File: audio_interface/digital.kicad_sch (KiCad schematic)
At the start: 45 parts, among them J10 MIC_EXT, J11 INST_EXT, J13 Test Headers, J14 SWD, J15 PCM_Jumper, J16 USB_B, SW1 SW_Push, U10 PCM4202, U11 STM32F042K6Tx

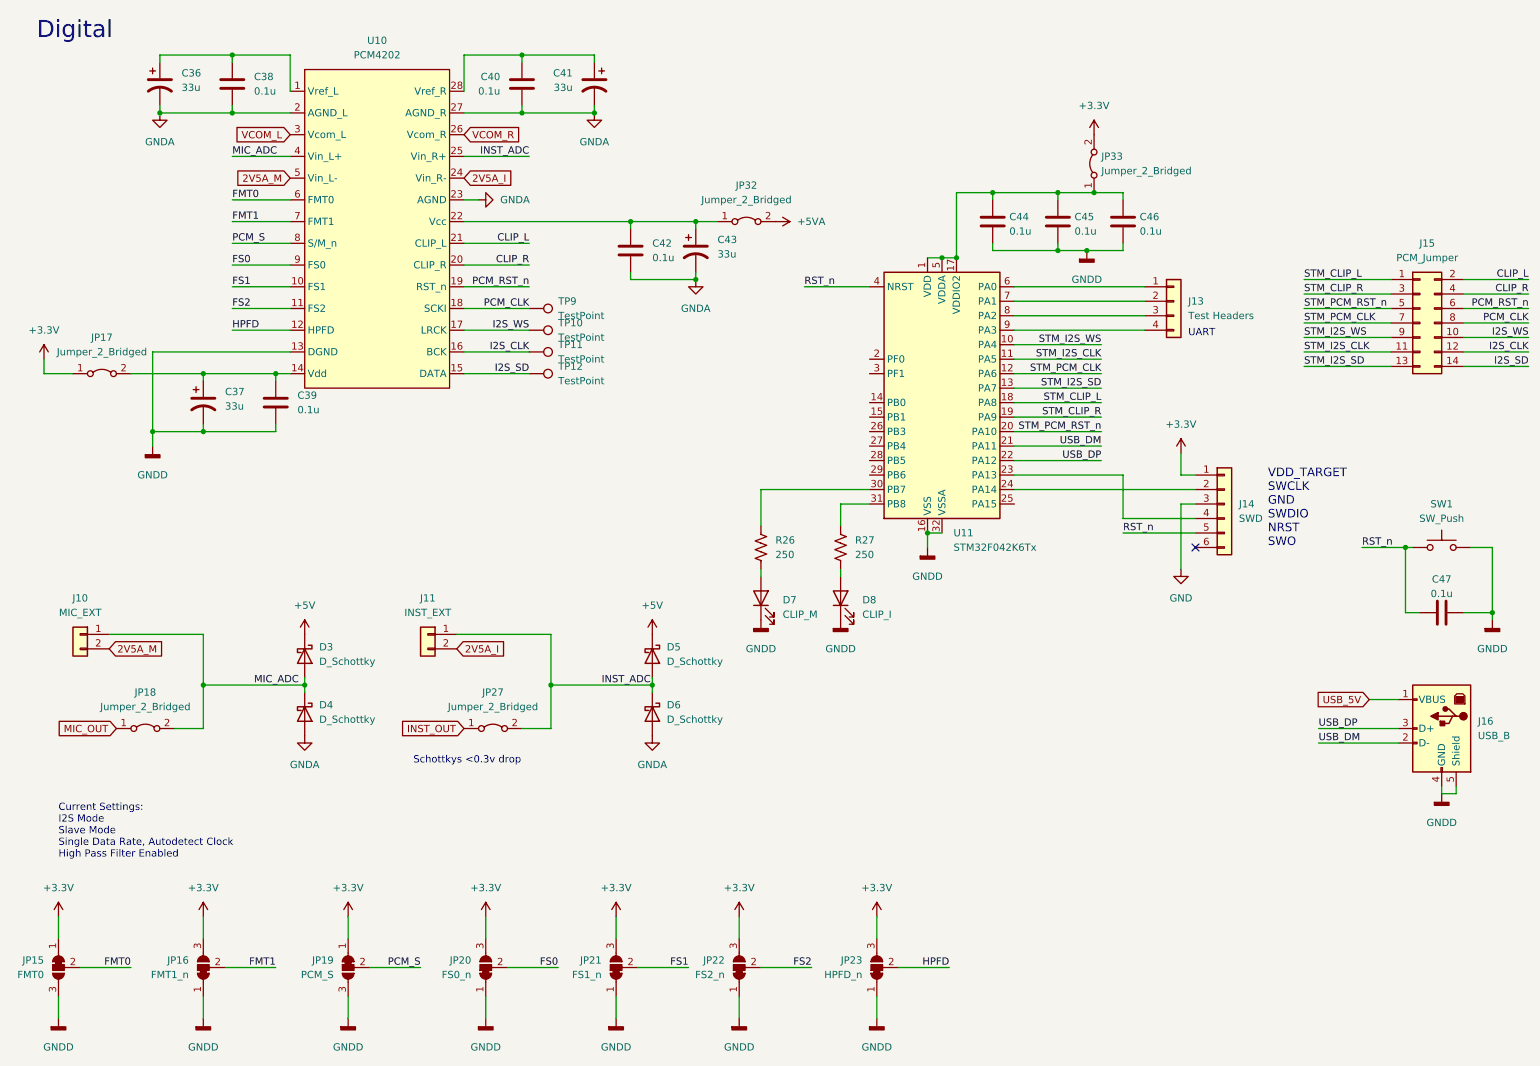
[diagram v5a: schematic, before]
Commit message: Fixed some layout issues. Flipped ADC.
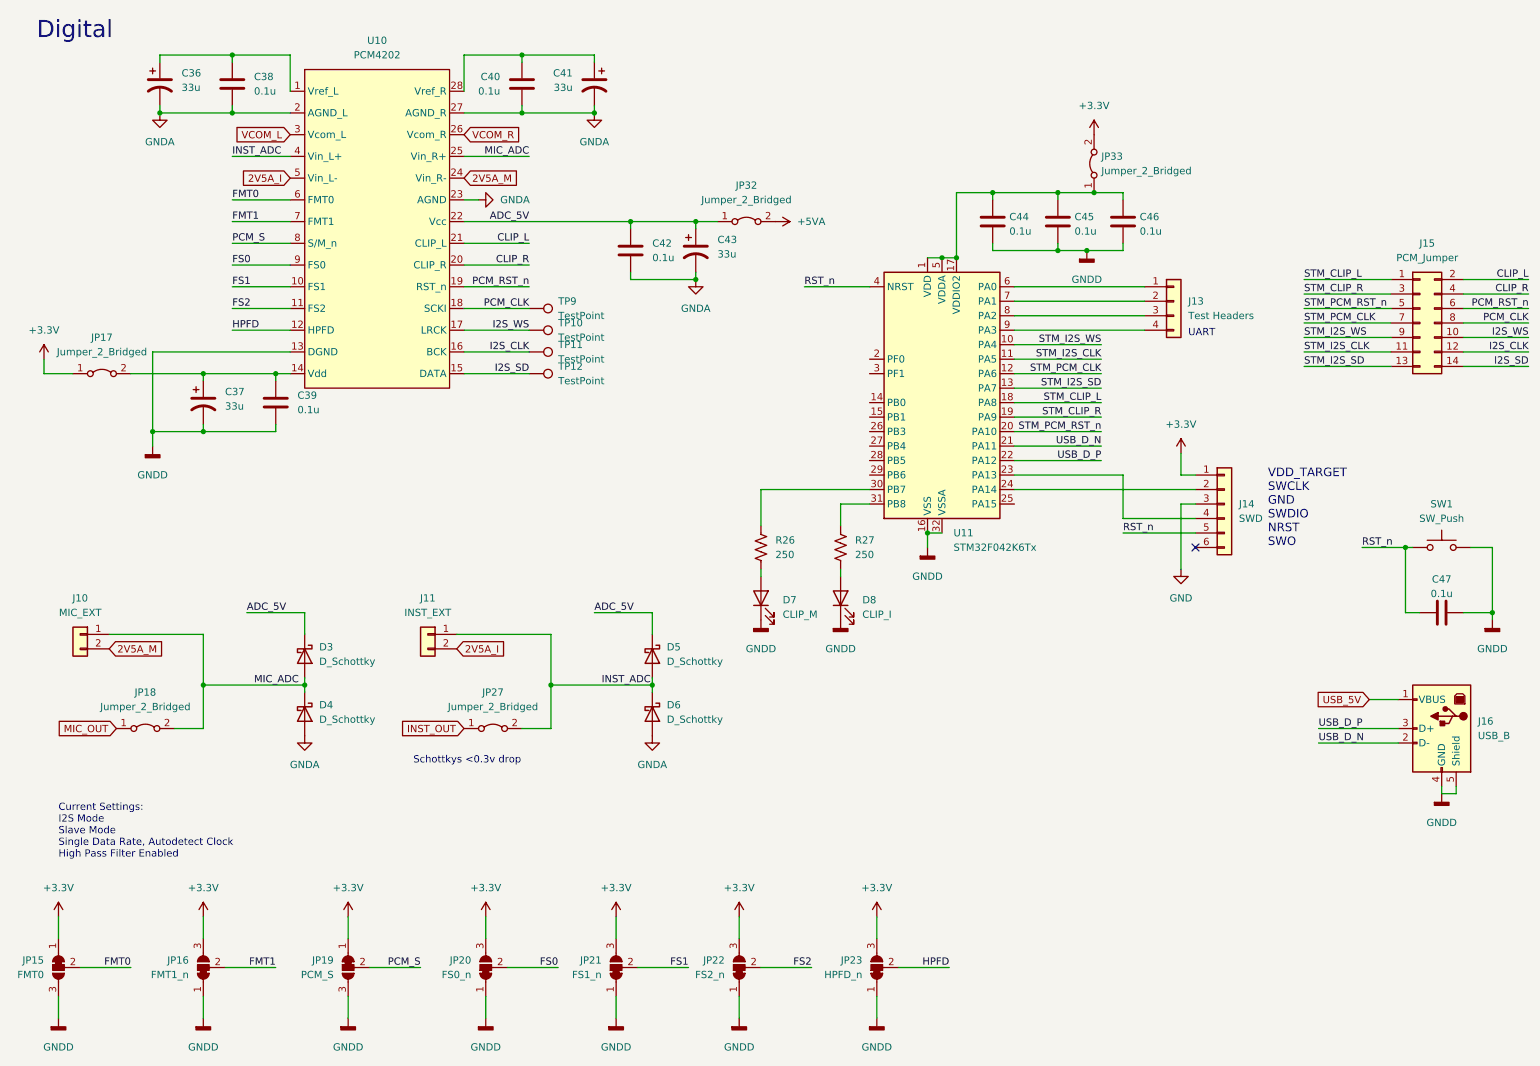
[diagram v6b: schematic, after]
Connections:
- net +5V is gone; now on net ADC_5V: D3.1 (K), D5.1 (K)
- net 2V5A_I: now also U10.5 (Vin_L-); no longer U10.24 (Vin_R-)
- net 2V5A_M: now also U10.24 (Vin_R-); no longer U10.5 (Vin_L-)
- net INST_ADC: now also U10.4 (Vin_L+); no longer U10.25 (Vin_R+)
- net MIC_ADC: now also U10.25 (Vin_R+); no longer U10.4 (Vin_L+)
- net ADC_5V: now reaches C42.1, C43.1, JP32.1 (A), U10.22 (Vcc)
- net USB_DM renamed USB_D_N
- net USB_DP renamed USB_D_P

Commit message: Changed pin mappings for easier layout. Redid layout for better ground plane.
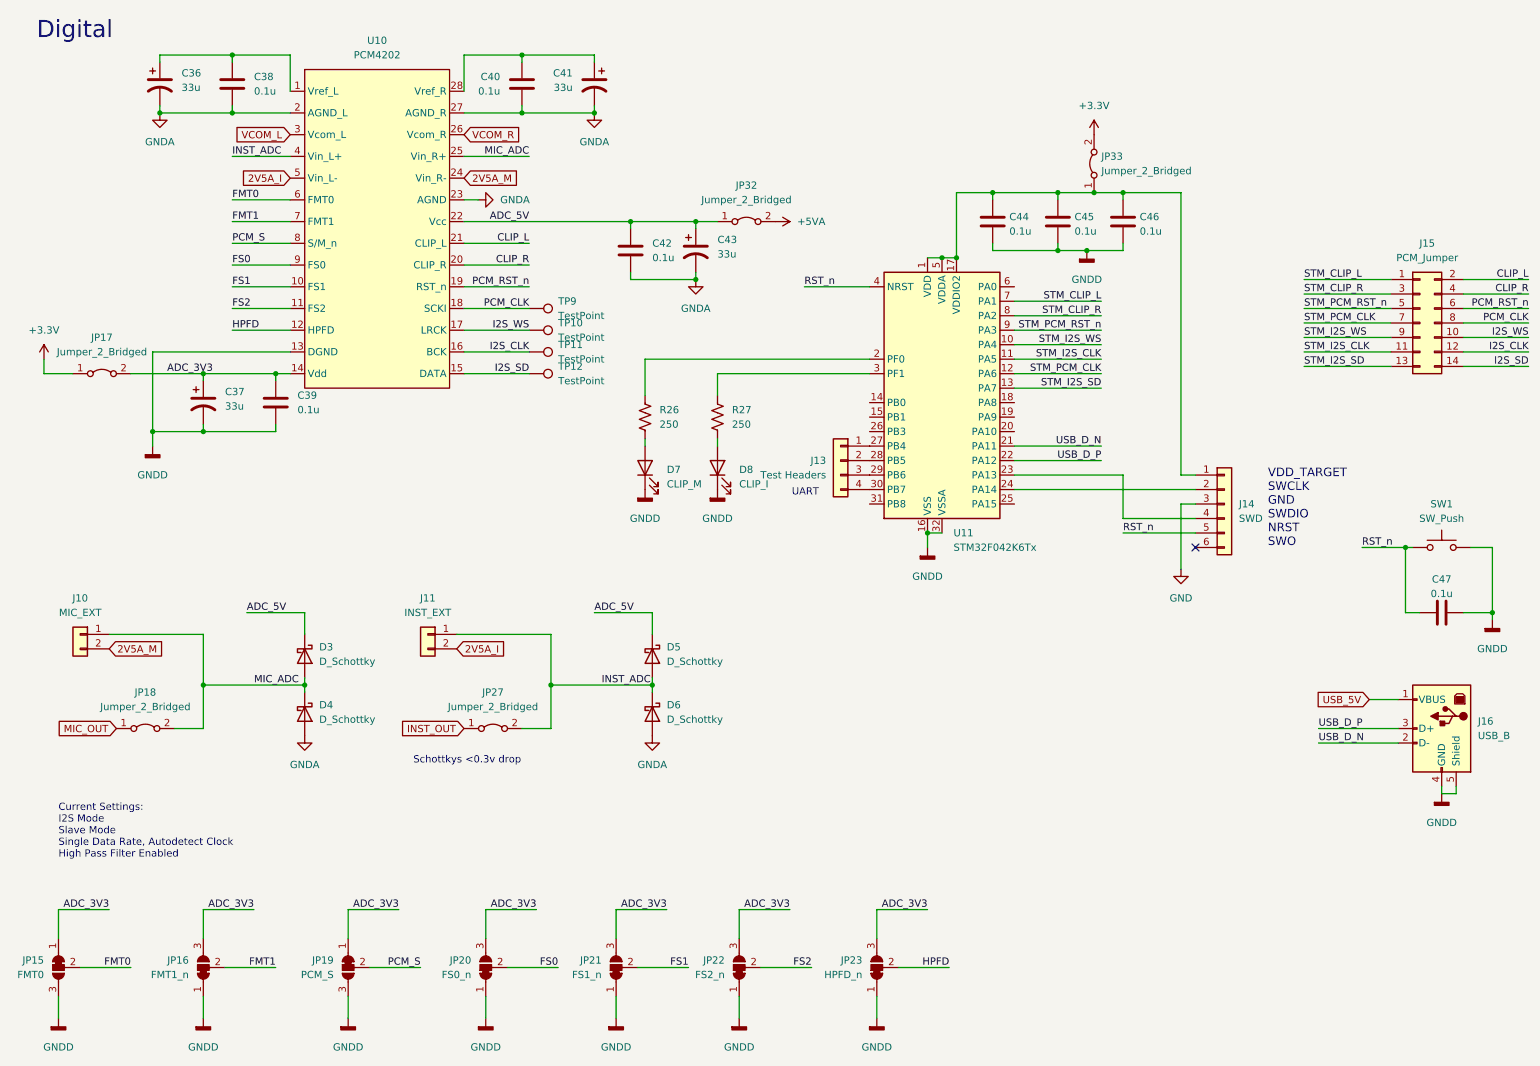
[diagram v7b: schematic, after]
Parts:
- C36, C37, C41, C43: footprint Capacitor_SMD:CP_Elec_6.3x5.2 -> Capacitor_SMD:CP_Elec_4x5.4
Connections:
- net +3V3: no longer J14.1 (Pin_1), JP15.1 (A), JP16.3 (B), JP19.1 (A), JP20.3 (B), JP21.3 (B), JP22.3 (B), JP23.3 (B)
- net STM_CLIP_L: now also U11.7 (PA1); no longer U11.18 (PA8)
- net STM_CLIP_R: now also U11.8 (PA2); no longer U11.19 (PA9)
- net STM_PCM_RST_n: now also U11.9 (PA3); no longer U11.20 (PA10)
- net ADC_3V3: now reaches C37.1, C39.1, JP17.2 (B), U10.14 (Vdd)
- net ADC_3V3: now also JP15.1 (A), JP16.3 (B), JP19.1 (A), JP20.3 (B), JP21.3 (B), JP22.3 (B), JP23.3 (B)
- net at C44.1, C45.1, C46.1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: now also J14.1 (Pin_1)
- net at U11.2 (PF0): now also R26.1
- net at U11.27 (PB4): now also J13.1 (Pin_1)
- net at U11.28 (PB5): now also J13.2 (Pin_2)
- net at U11.29 (PB6): now also J13.3 (Pin_3)
- net at U11.3 (PF1): now also R27.1
- net at U11.30 (PB7): now also J13.4 (Pin_4); no longer R26.1
- net at U11.31 (PB8): no longer R27.1
- net at U11.6 (PA0): no longer J13.1 (Pin_1)
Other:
- moved on the sheet: D7, D8, J13, R26, R27
